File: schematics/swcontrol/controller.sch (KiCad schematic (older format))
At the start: 7 parts, among them P1 BK24x1, P2 BSL, P3 PWRBRD, U1 MSP430F1222IDW

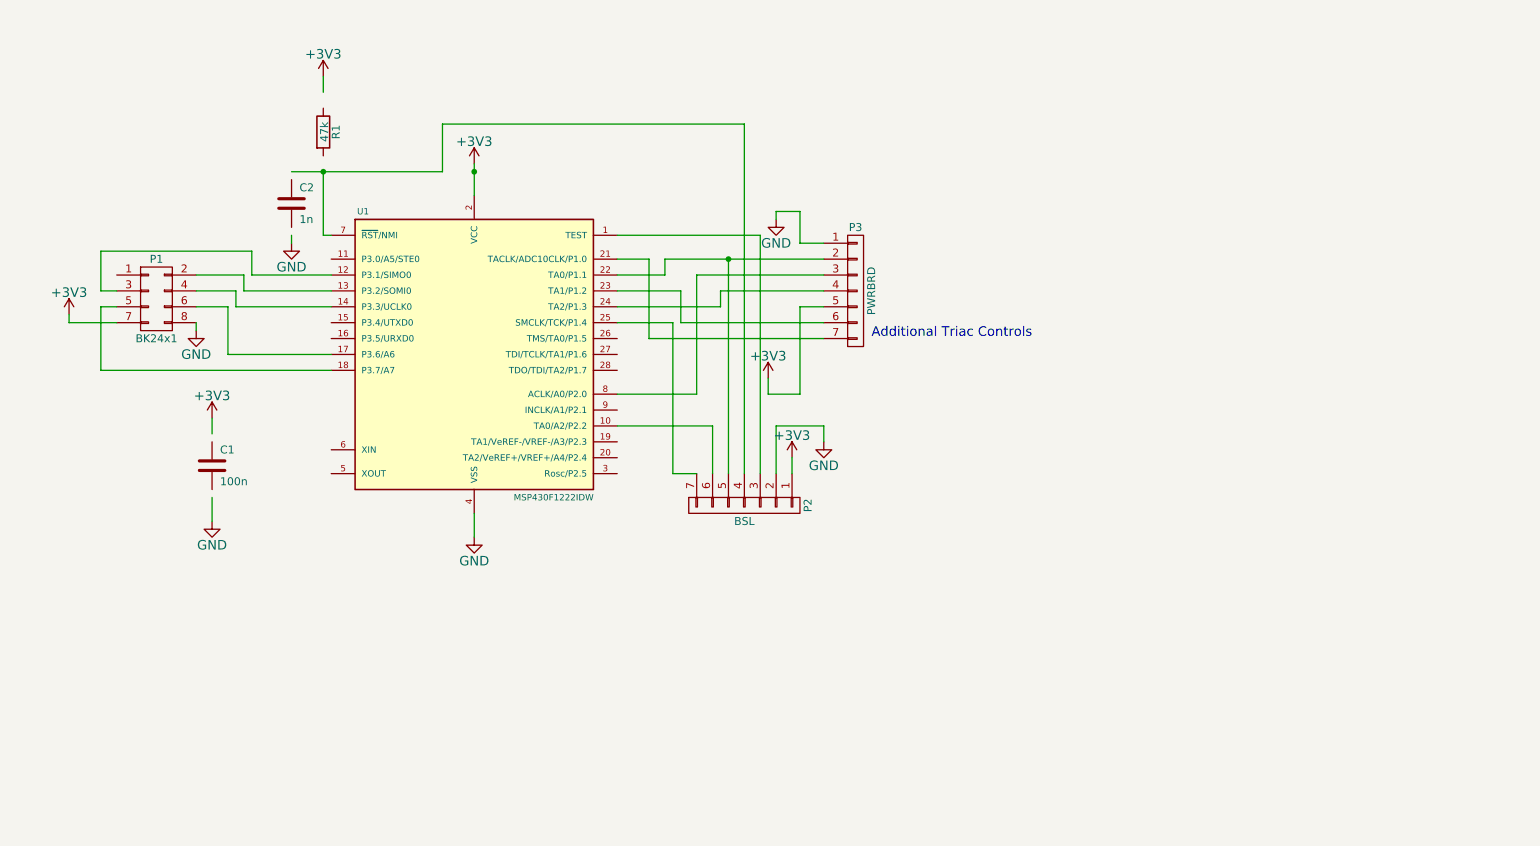
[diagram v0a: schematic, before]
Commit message: Changing uC
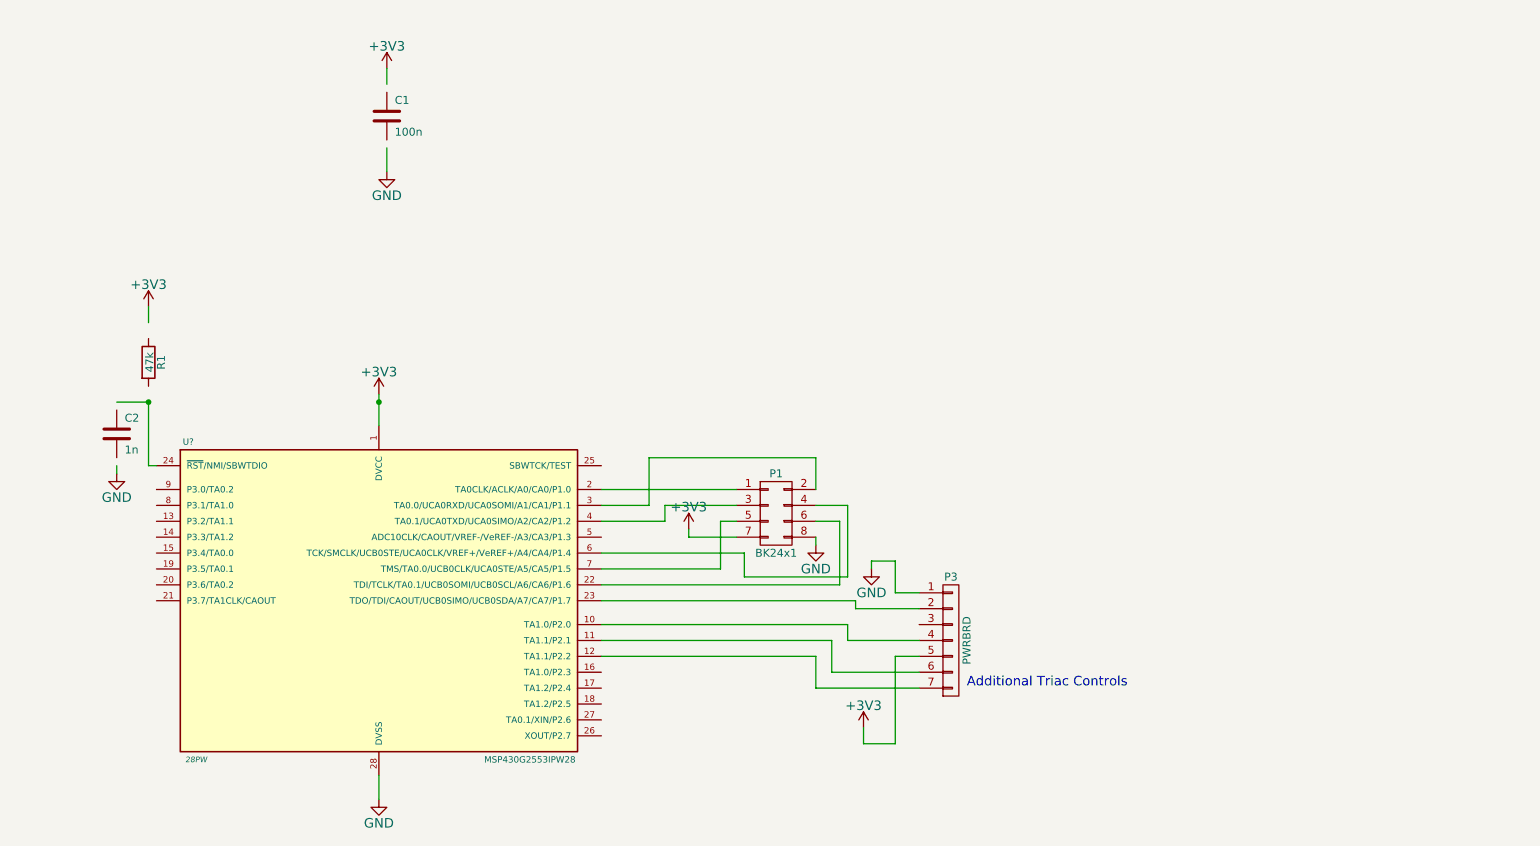
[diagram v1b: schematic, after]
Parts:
- removed P2: BSL, Pin_Headers:Pin_Header_Straight_1x07, symbol CONN_01X07
- removed U1: MSP430F1222IDW, SMD_Packages:SSOP-28, symbol MSP430F1222IDW
- added U?: MSP430G2553IPW28, 28PW, symbol MSP430G2553IPW28
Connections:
- wire segments 67 -> 51
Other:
- moved on the sheet: C1, C2, P1, P3, R1

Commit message: Fixed schematics
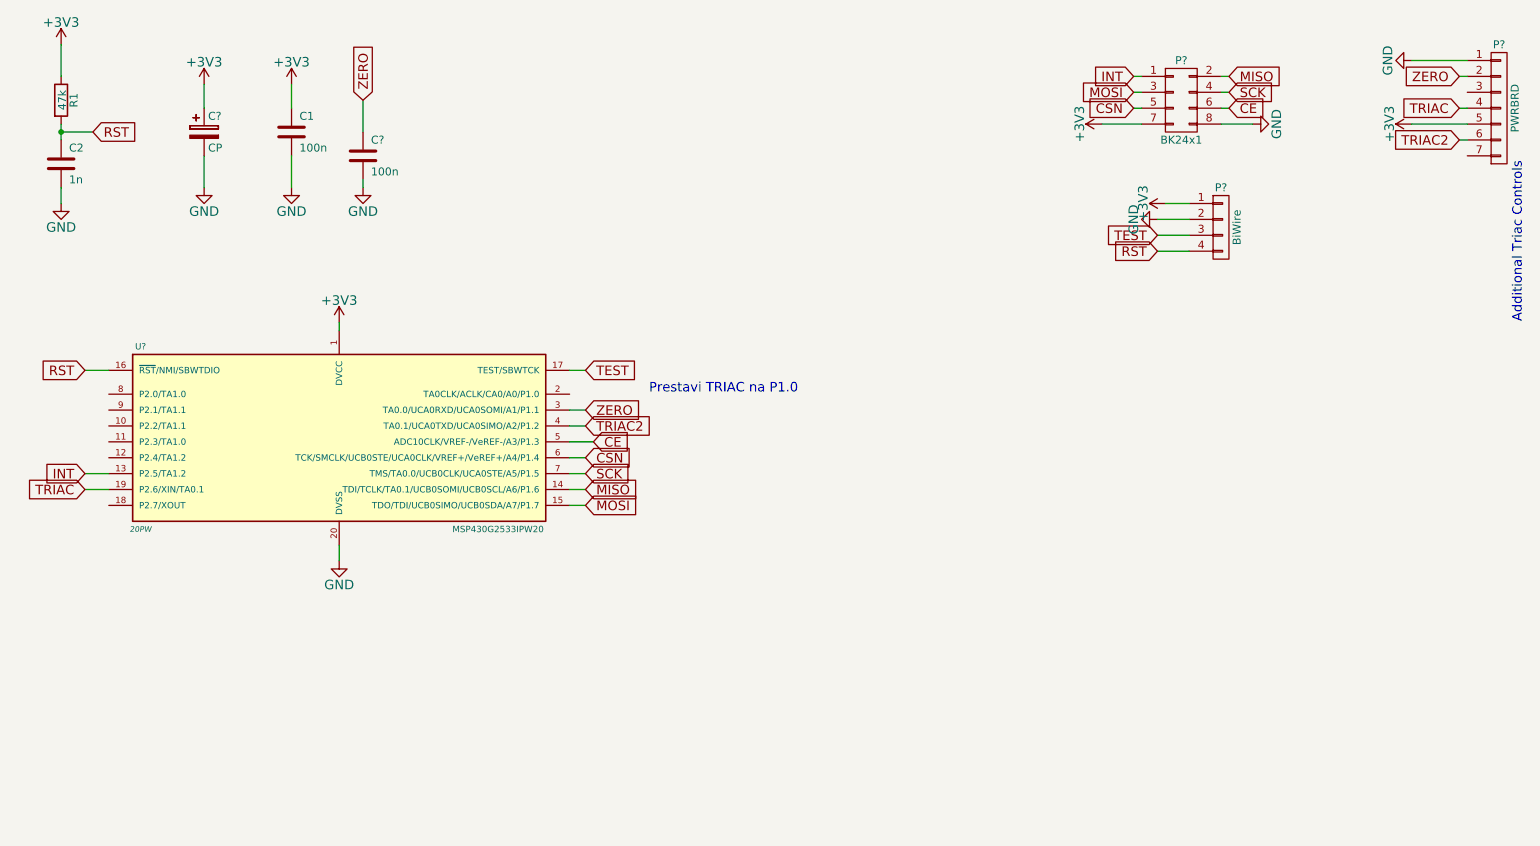
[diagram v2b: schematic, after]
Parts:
- removed P1: BK24x1, Pin_Headers:Pin_Header_Straight_2x04, symbol CONN_02X04
- removed P3: PWRBRD, Pin_Headers:Pin_Header_Straight_1x07, symbol CONN_01X07
- removed U?: MSP430G2553IPW28, 28PW, symbol MSP430G2553IPW28
- added C?: CP, symbol CP
- added C?: 100n, Capacitors_SMD:C_0805, symbol C
- added P?: BK24x1, Pin_Headers:Pin_Header_Straight_2x04, symbol CONN_02X04
- added P?: BiWire, symbol CONN_01X04
- added P?: PWRBRD, Pin_Headers:Pin_Header_Straight_1x07, symbol CONN_01X07
- added U?: MSP430G2533IPW20, 20PW, symbol MSP430G2533IPW20
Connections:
- net labels added: CE, CSN, INT, MISO, MOSI, RST, SCK, TEST, TRIAC, TRIAC2, ZERO
- wire segments 51 -> 40
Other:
- note added: "Prestavi TRIAC na P1.0\n"
- moved on the sheet: C1, C2, R1

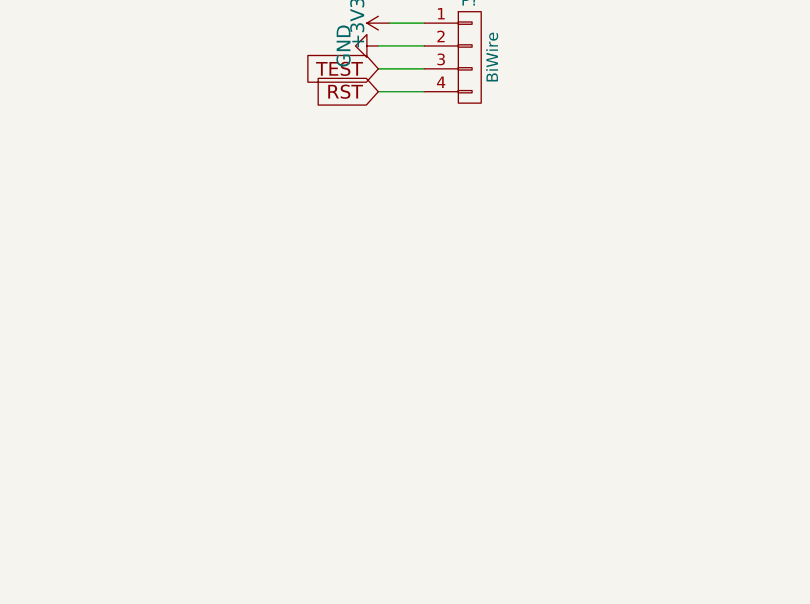
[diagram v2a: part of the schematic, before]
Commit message: Mini transceiver added on board
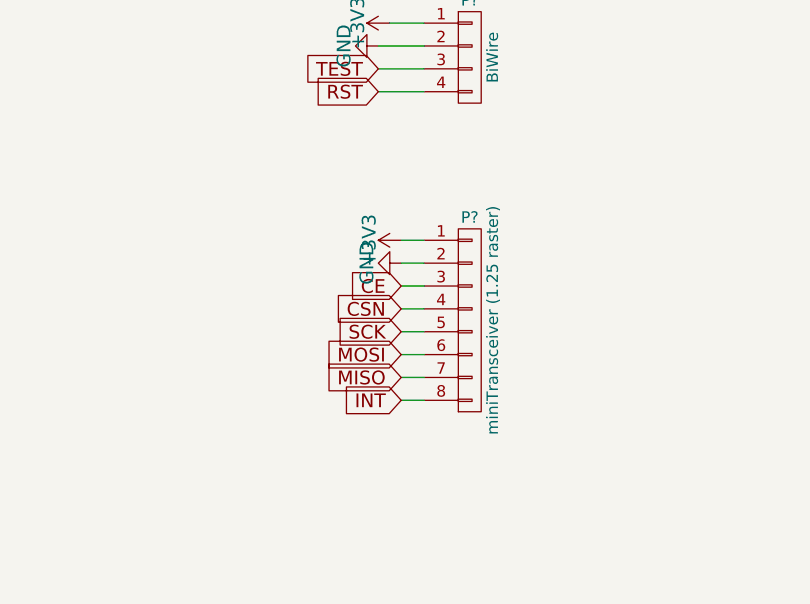
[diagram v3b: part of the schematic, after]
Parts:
- added P?: miniTransceiver (1.25 raster), symbol CONN_01X08
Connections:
- net +3V3: now also P?.1 (P1)
- net CE: now also P?.3 (P3)
- net CSN: now also P?.4 (P4)
- net GND: now also P?.2 (P2)
- net INT: now also P?.8 (P8)
- net MISO: now also P?.7 (P7)
- net MOSI: now also P?.6 (P6)
- net SCK: now also P?.5 (P5)
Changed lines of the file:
@@
 Wire Wire Line
 	8350 1050 8300 1050
+$Comp
+L CONN_01X08 P?
+U 1 1 55486003
+P 8850 3150
+F 0 "P?" H 8850 3600 50  0000 C CNN
+F 1 "miniTransceiver (1.25 raster)" V 8950 3150 50  0000 C CNN
+F 2 "" H 8850 3150 60  0000 C CNN
+F 3 "" H 8850 3150 60  0000 C CNN
+	1    8850 3150
+	1    0    0    -1
+$EndComp
+$Comp
+L +3V3 #PWR?
+U 1 1 55486133
+P 8550 2800
+F 0 "#PWR?" H 8550 2650 60  0001 C CNN
+F 1 "+3V3" H 8550 2940 60  0000 C CNN
+F 2 "" H 8550 2800 60  0000 C CNN
+F 3 "" H 8550 2800 60  0000 C CNN
+	1    8550 2800
+	0    -1   -1   0
+$EndComp
+$Comp
+L GND #PWR?
+U 1 1 5548615C
+P 8550 2900
+F 0 "#PWR?" H 8550 2650 60  0001 C CNN
+F 1 "GND" H 8550 2750 60  0000 C CNN
+F 2 "" H 8550 2900 60  0000 C CNN
+F 3 "" H 8550 2900 60  0000 C CNN
+	1    8550 2900
+	0    1    1    0
+$EndComp
+Text GLabel 8550 3000 0    60   Input ~ 0
+CE
+Text GLabel 8550 3100 0    60   Input ~ 0
+CSN
+Text GLabel 8550 3200 0    60   Input ~ 0
+SCK
+Text GLabel 8550 3300 0    60   Input ~ 0
+MOSI
+Text GLabel 8550 3400 0    60   Input ~ 0
+MISO
+Text GLabel 8550 3500 0    60   Input ~ 0
+INT
+Wire Wire Line
+	8550 3000 8650 3000
+Wire Wire Line
+	8550 3100 8650 3100
+Wire Wire Line
+	8550 3200 8650 3200
+Wire Wire Line
+	8550 3300 8650 3300
+Wire Wire Line
+	8550 3400 8650 3400
+Wire Wire Line
+	8550 3500 8650 3500
+Wire Wire Line
+	8550 2900 8650 2900
+Wire Wire Line
+	8550 2800 8650 2800
 $EndSCHEMATC
